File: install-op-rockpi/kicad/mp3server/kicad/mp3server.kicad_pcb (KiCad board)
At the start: 2 copper layers, 101.6 x 76.2 mm, 28 parts, among them J1 Conn_01x02, J2 USB_2, P1 CONN_1, P10 CONN_1, P11 CONN_1, P12 CONN_1, P13 CONN_1, P14 CONN_1, P15 CONN_1, P16 CONN_1, P17 CONN_1, P18 CONN_1, P19 CONN_1, P2 CONN_1, P3 ROCKPI_S, P4 CONN_5, P5 CONN_5, P6 CONN_3, P7 CONN_4X1, P8 ROCKPI_S_H2

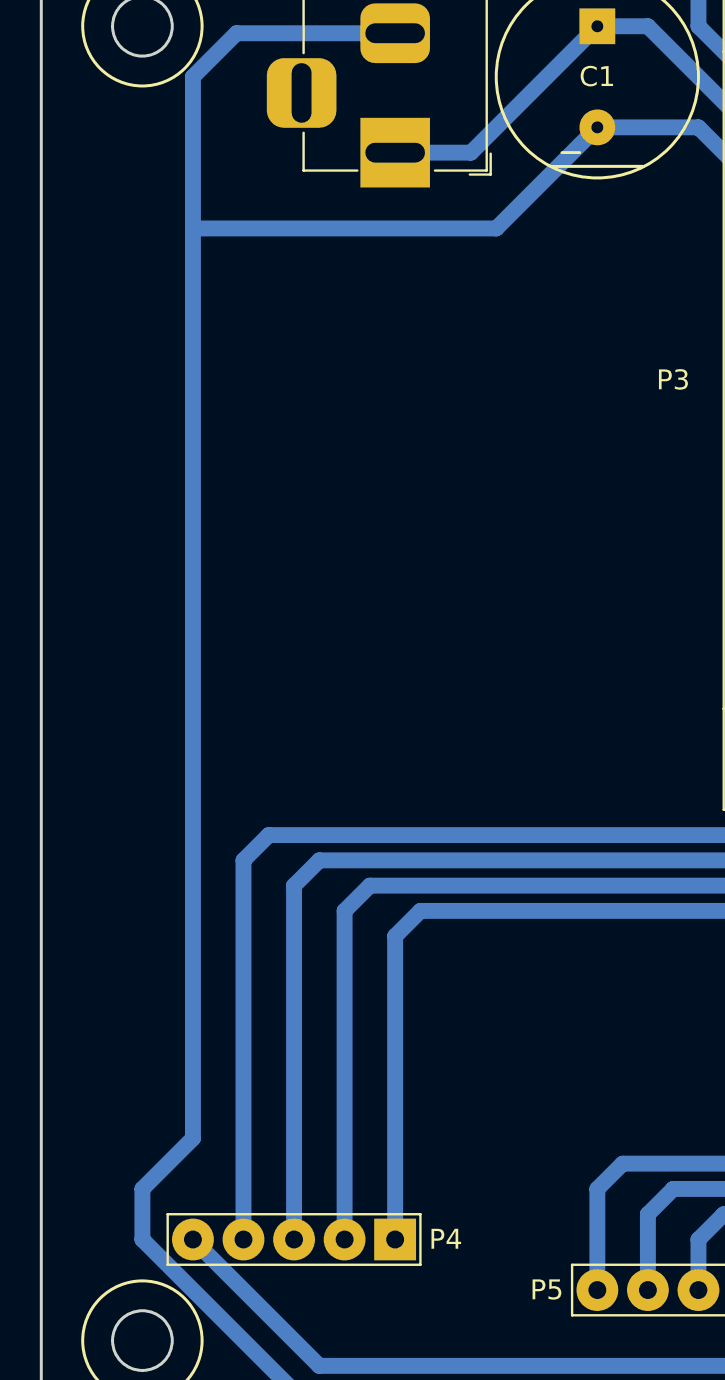
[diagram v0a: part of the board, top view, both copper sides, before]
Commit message: change repo dirs
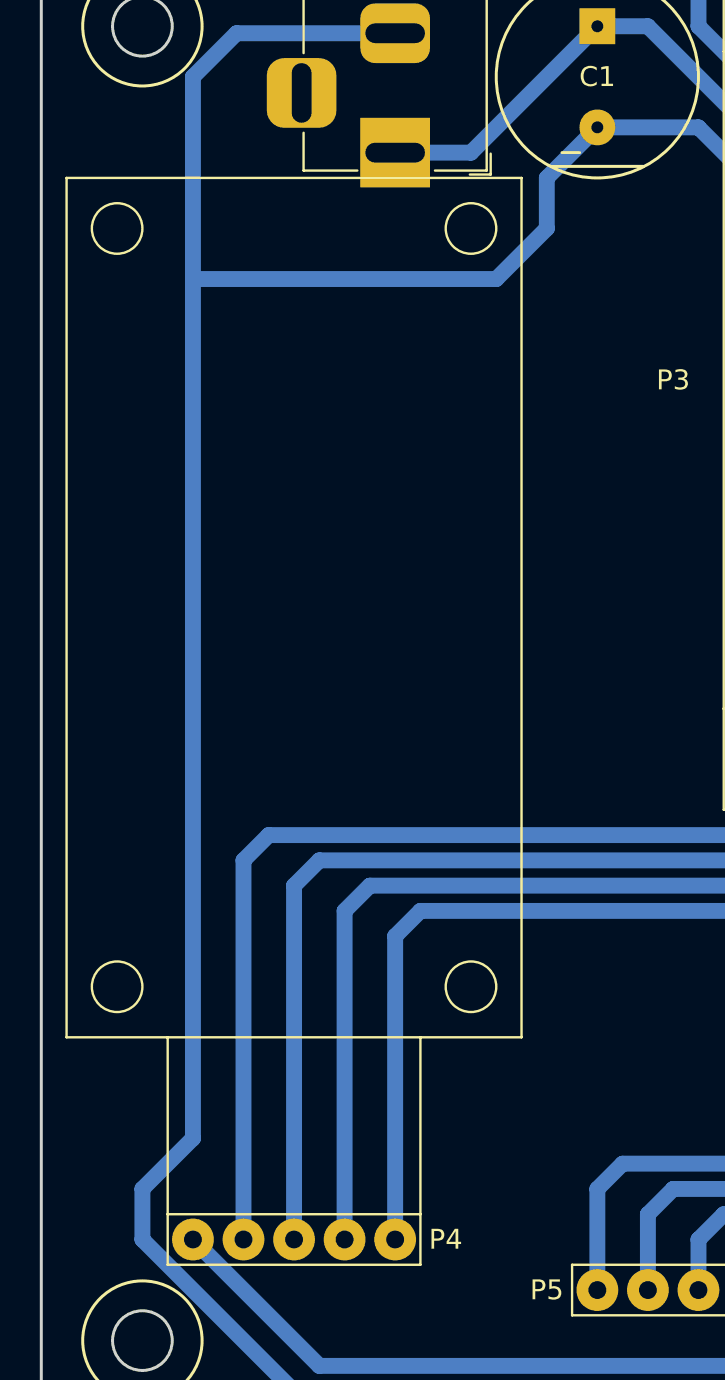
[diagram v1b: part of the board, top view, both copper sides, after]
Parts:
- P4: footprint kicad:PIN_ARRAY_5X1 -> kicad:VMA301
- turned P4 to 0 degrees
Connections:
- P4 pad 1: Net-(P3-Pad19) -> Net-(P3-Pad1)
- P4 pad 2: Net-(P3-Pad21) -> Net-(P3-Pad25)
- P4 pad 4: Net-(P3-Pad25) -> Net-(P3-Pad21)
- P4 pad 5: Net-(P3-Pad1) -> Net-(P3-Pad19)
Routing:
- net Net-(C1-Pad2): track 274.9 -> 277.4 mm

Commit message: armbian kernel update
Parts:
- added C2: CP1, kicad:CP2, F.Cu at (129.5, 154.9)
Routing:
- net Net-(C1-Pad2): track 277.4 -> 281.5 mm
- net Net-(C2-Pad1): track 142.8 -> 145.4 mm

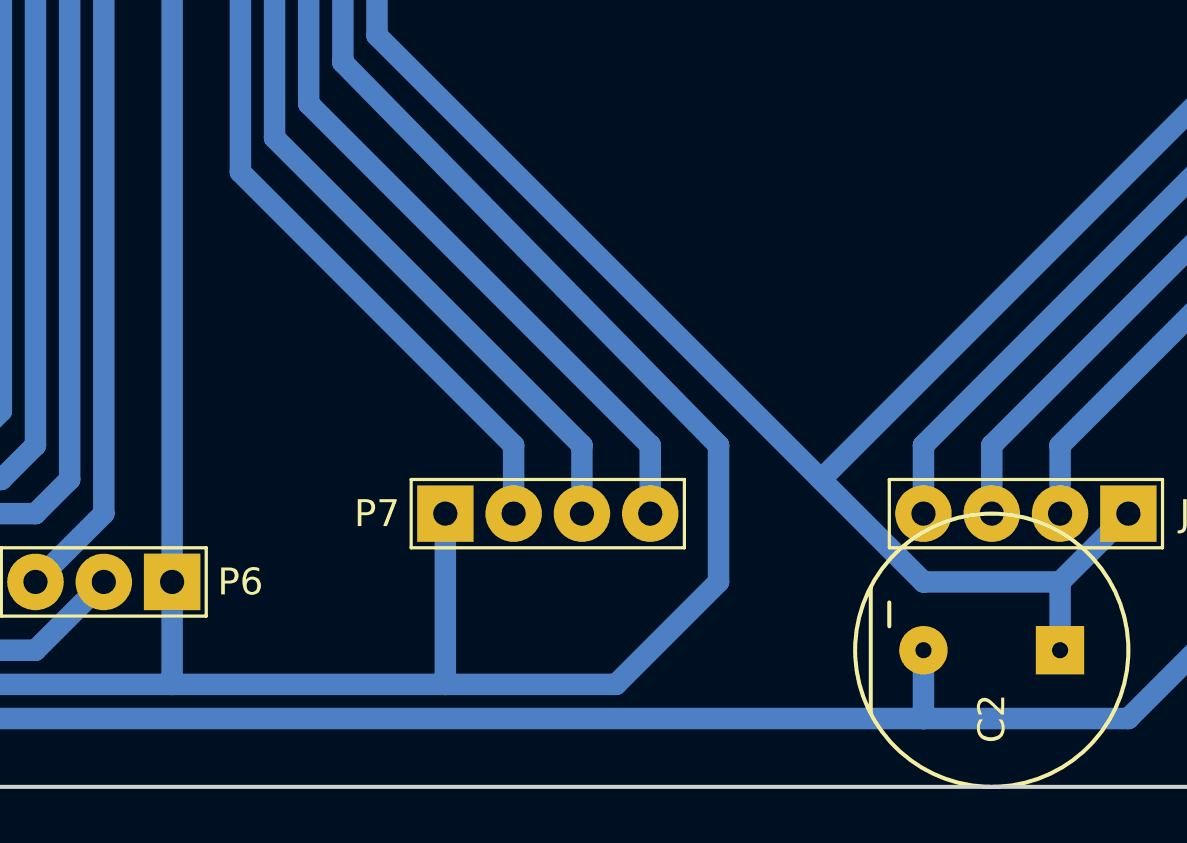
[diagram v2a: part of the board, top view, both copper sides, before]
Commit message: oled: change gnd and vcc pins order
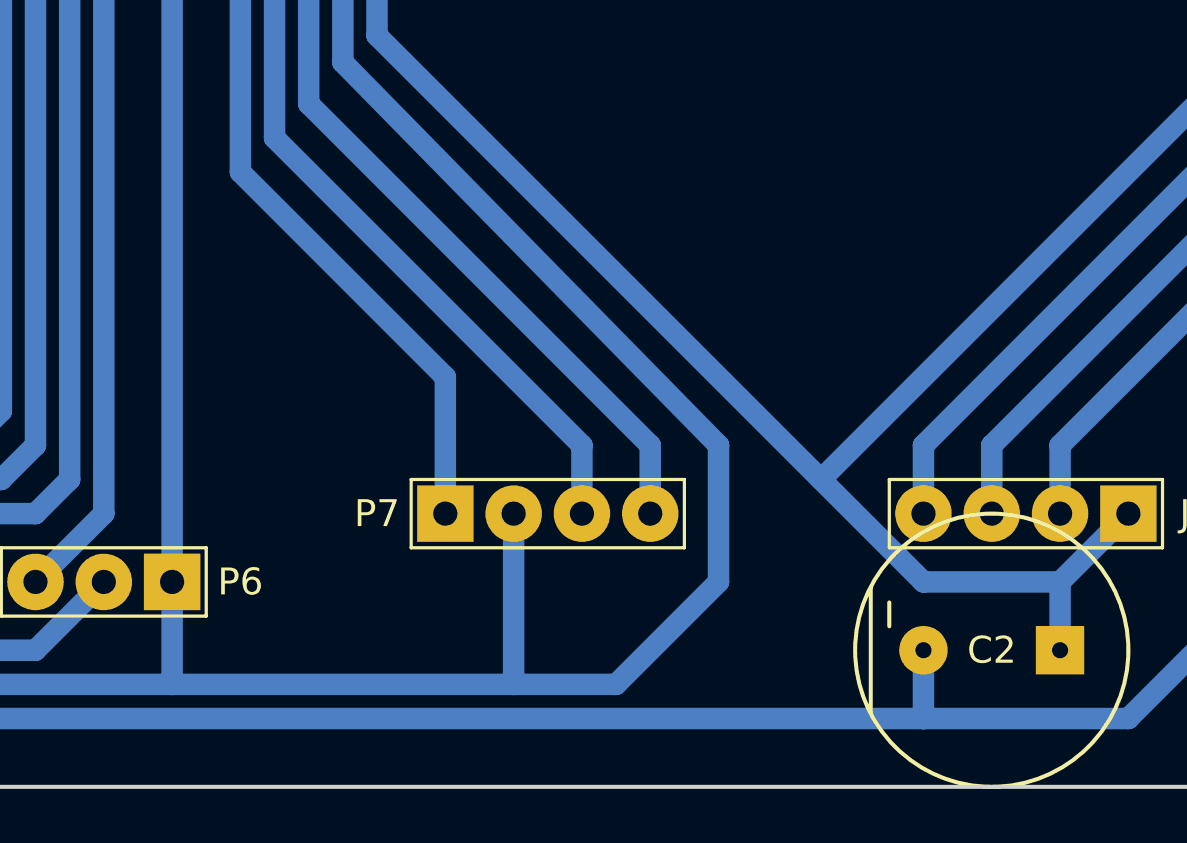
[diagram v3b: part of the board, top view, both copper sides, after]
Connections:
- P7 pad 1: Net-(P3-Pad1) -> Net-(P3-Pad9)
- P7 pad 2: Net-(P3-Pad9) -> Net-(P3-Pad1)
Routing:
- net Net-(P3-Pad9): track 146.1 -> 145.0 mm
